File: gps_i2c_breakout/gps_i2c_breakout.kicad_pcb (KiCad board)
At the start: 2 copper layers, 38.2 x 13 mm, 7 parts, among them J1 Conn_01x02_Male, J2 Conn_01x04_Male, J3 Conn_01x04_Male, J4 Conn_01x04_Male, J5 Conn_01x04_Male, J7 5V, J8 GND

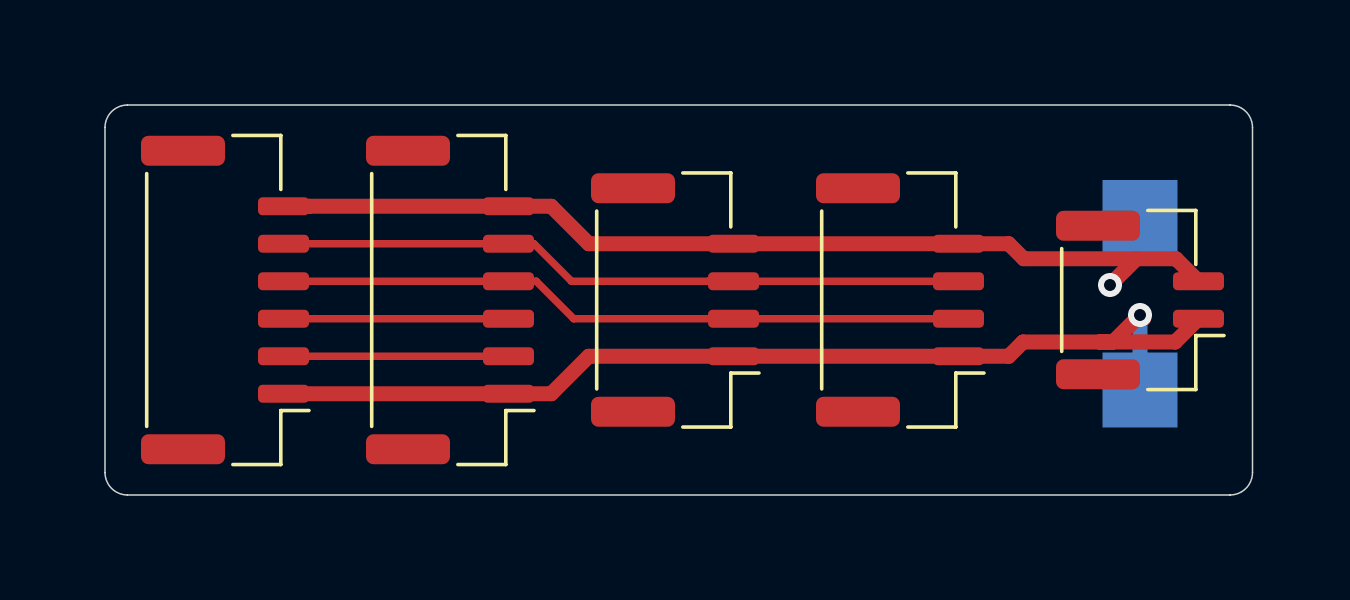
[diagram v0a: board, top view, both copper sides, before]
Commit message: Updated the I2C and GPS breakout boards with ground fills
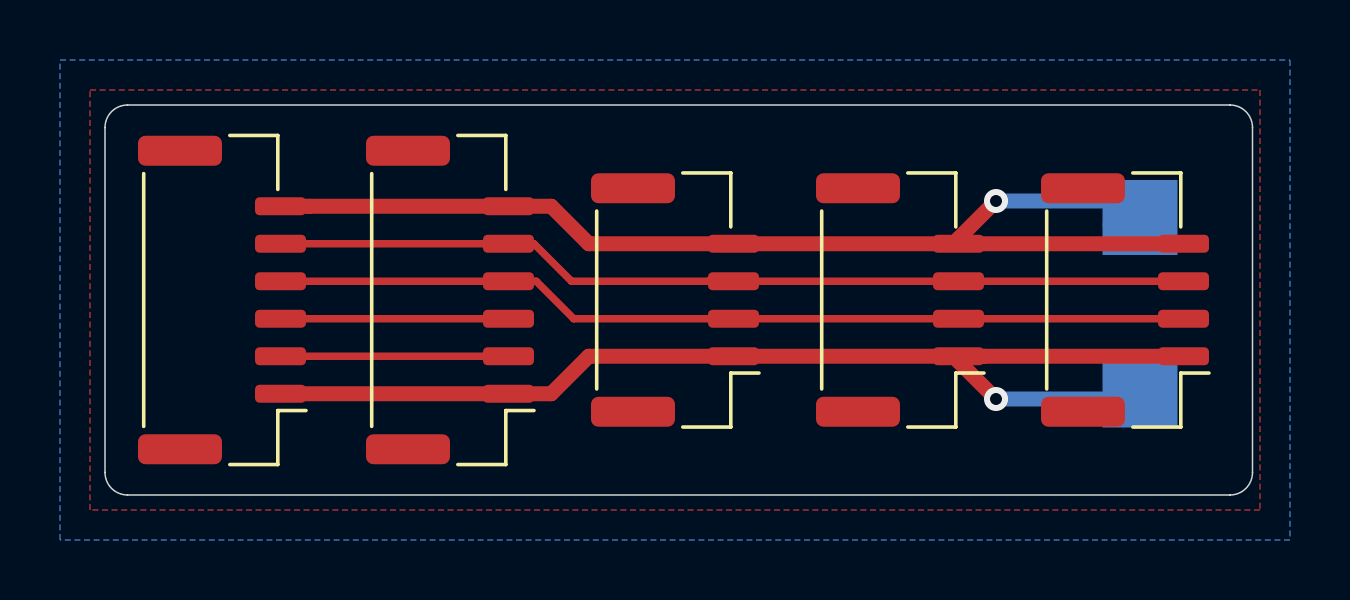
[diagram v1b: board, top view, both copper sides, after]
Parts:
- removed J1: Conn_01x02_Male, Connector_JST:JST_GH_BM02B-GHS-TBT_1x02-1MP_P1.25mm_Vertical
- added J6: Conn_01x06_Male, Connector_JST:JST_GH_BM06B-GHS-TBT_1x06-1MP_P1.25mm_Vertical, F.Cu at (179.4, 75.0)
- J4: footprint Connector_JST:JST_GH_BM06B-GHS-TBT_1x06-1MP_P1.25mm_Vertical -> Connector_JST:JST_GH_BM04B-GHS-TBT_1x04-1MP_P1.25mm_Vertical
- J5: value Conn_01x04_Male -> Conn_01x06_Male
- moved J4 30.0 mm to (209.5, 75.0)
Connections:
- J4 pad 2: Net-(J4-Pad2) -> Net-(J2-Pad2)
- J4 pad 3: Net-(J4-Pad3) -> Net-(J2-Pad3)
- J4 pad 4: Net-(J2-Pad2) -> Earth
- J5 pad 2: Net-(J4-Pad2) -> Net-(J5-Pad2)
- J5 pad 3: Net-(J4-Pad3) -> Net-(J5-Pad3)
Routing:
- net Net-(J5-Pad3): track 0.00 -> 7.50 mm
- net Net-(J5-Pad2): track 0.00 -> 7.50 mm
- net Net-(J4-Pad3): track 7.50 -> 0.00 mm
- net Net-(J4-Pad2): track 7.50 -> 0.00 mm
- net Net-(J2-Pad3): track 23.0 -> 30.5 mm
- net Net-(J2-Pad2): track 23.0 -> 30.5 mm
- net Earth: track 36.9 -> 38.9 mm
- net +5V: track 35.9 -> 37.4 mm
- added copper zone on B.Cu, net Earth
- added copper zone on F.Cu, net Earth
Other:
- board text added: "GPS / I2C Breakout v2 MA - 2022"
- board text removed: "GPS / I2C Breakout v1 MA - 2021"
